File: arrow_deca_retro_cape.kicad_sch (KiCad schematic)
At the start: 48 parts, among them J1 ZXSP_ED2X28_SPE_SOL_EDGE, J10 Conn_02x05_Odd_Even, J11 Conn_01x04, J12 Conn_01x03, J13 Conn_01x01, J14 Conn_01x02, J15 Conn_01x03, J16 Conn_01x06, J2 Conn_01x03, J3 Conn_01x03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

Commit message: added Deto pmod
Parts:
- J16: footprint (none) -> Connector_PinHeader_2.54mm:PinHeader_1x06_P2.54mm_Vertical
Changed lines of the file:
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@@
   (symbol (lib_id "power:+3V3") (at 111.76 139.7 0) (unit 1)
     (in_bom yes) (on_board yes)
-    (property "Reference" "#PWR?" (id 0) (at 111.76 143.51 0)
+    (property "Reference" "#PWR031" (id 0) (at 111.76 143.51 0)
       (effects (font (size 1.27 1.27)) hide)
     )
@@
       (effects (font (size 1.27 1.27)) (justify left))
     )
-    (property "Footprint" "" (id 2) (at 118.745 147.32 0)
+    (property "Footprint" "Connector_PinHeader_2.54mm:PinHeader_1x06_P2.54mm_Vertical" (id 2) (at 118.745 147.32 0)
       (effects (font (size 1.27 1.27)) hide)
     )
@@
       (reference "#PWR030") (unit 1) (value "+2V5") (footprint "")
     )
+    (path "/2c197801-fcda-427b-8b74-c13df53c8843"
+      (reference "#PWR031") (unit 1) (value "+3V3") (footprint "")
+    )
     (path "/a40aa6c1-da40-4892-8d84-7e2be4c1f25d"
       (reference "#PWR0101") (unit 1) (value "GND") (footprint "")
@@
       (reference "#PWR0122") (unit 1) (value "GNDA") (footprint "")
     )
-    (path "/2c197801-fcda-427b-8b74-c13df53c8843"
-      (reference "#PWR?") (unit 1) (value "+3V3") (footprint "")
-    )
     (path "/00000000-0000-0000-0000-000061566687"
       (reference "C1") (unit 1) (value "1uF") (footprint "Capacitor_SMD:C_0603_1608Metric_Pad1.05x0.95mm_HandSolder")
@@
     )
     (path "/7d86abca-ab79-4536-9060-e252a4e431a0"
-      (reference "J16") (unit 1) (value "Conn_01x06") (footprint "")
+      (reference "J16") (unit 1) (value "Conn_01x06") (footprint "Connector_PinHeader_2.54mm:PinHeader_1x06_P2.54mm_Vertical")
     )
     (path "/439aafdc-2c0e-44db-ab96-7212e6daa700"

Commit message: v0.5 routing finalized
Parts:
- removed J11: Conn_01x04, Connector_PinSocket_2.54mm:PinSocket_1x04_P2.54mm_Vertical, symbol Connector_Generic:Conn_01x04
- added C21: 100uF, Capacitor_SMD:C_0805_2012Metric_Pad1.18x1.45mm_HandSolder, symbol Device:C
- added J11: USB_A, Connector_USB:USB_A_Molex_67643_Horizontal, symbol Connector:USB_A
- C20: value 0.1uF -> 10uF
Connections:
- net +2V5: now also C21.1
- net +5V: now also J11.1 (VBUS)
- net GND: now also C21.2, J11.4 (GND), J11.5 (Shield)
- net PS2_KEYB_CLK: now also R1.1; no longer R2.1
- net PS2_KEYB_DAT: now also R2.1; no longer R1.1
- net USB_D-_DM: now reaches D1.3, R2.2, R3.1
- net USB_D-_DM: now also J11.2 (D-)
- net USB_D+_DP: now reaches D2.3, R1.2, R4.1
- net USB_D+_DP: now also J11.3 (D+)
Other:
- note added: "- LOGOS I SILKSCREEN FRONT/BACK - USB3 SERIAL - REVISAR PINOUT I2S"
- note added: "USB"
- note removed: "ALTERNATIVA AMS1117-3V3 1A"
- note removed: "D+ / DP"
- note removed: "D- / DM"
- note removed: "UNIFICAR CONDENSADORS 0805 A 0603"
- note removed: "USB Header"
- company: (none) -> Hard Team Deca
- title: (none) -> DECA RETRO CAPE 1
- moved on the sheet: J10, J13, J14, J15

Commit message: update before split
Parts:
- removed J11: USB_A, Connector_USB:USB_A_Molex_67643_Horizontal, symbol Connector:USB_A
- R1, R2: value 510 -> 120; Field4 (none) -> Antonio entre 120 i 180 Ohm (47 també)
- R3, R4: value 4k7 -> NC
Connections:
- net +3V3: no longer J5.4
- net +5V: now also J5.4
- net PS2_KEYB_CLK: no longer J5.5
- net PS2_KEYB_DAT: no longer J5.1
- net USB_D+_DP: no longer names the net of D2.3, R1.2, R4.1
- net USB_D+_DP: now also J5.5
- net USB_D-_DM: no longer names the net of D1.3, R2.2, R3.1
- net USB_D-_DM: now also J5.1
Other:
- note added: "- REVISAR PINOUT, i2s retorn deca a DAC DETO 2, 3, 4 - USB3 SERIAL - I2S header al DETO PMOD - PS2 MOUSE connector - PULL DOWN PS2 GND POSAR A SORTIDES FPGA - REVISAR PULL DOWN CKE"
- note added: "BCLK"
- note added: "D+_DP"
- note added: "D-_DM"
- note added: "DIN"
- note added: "LRCLK"
- note removed: "- LOGOS I SILKSCREEN FRONT/BACK - USB3 SERIAL - REVISAR PINOUT I2S"
- note removed: "USB"
- moved on the sheet: D1, D2, J5, R1, R2, R3, R4

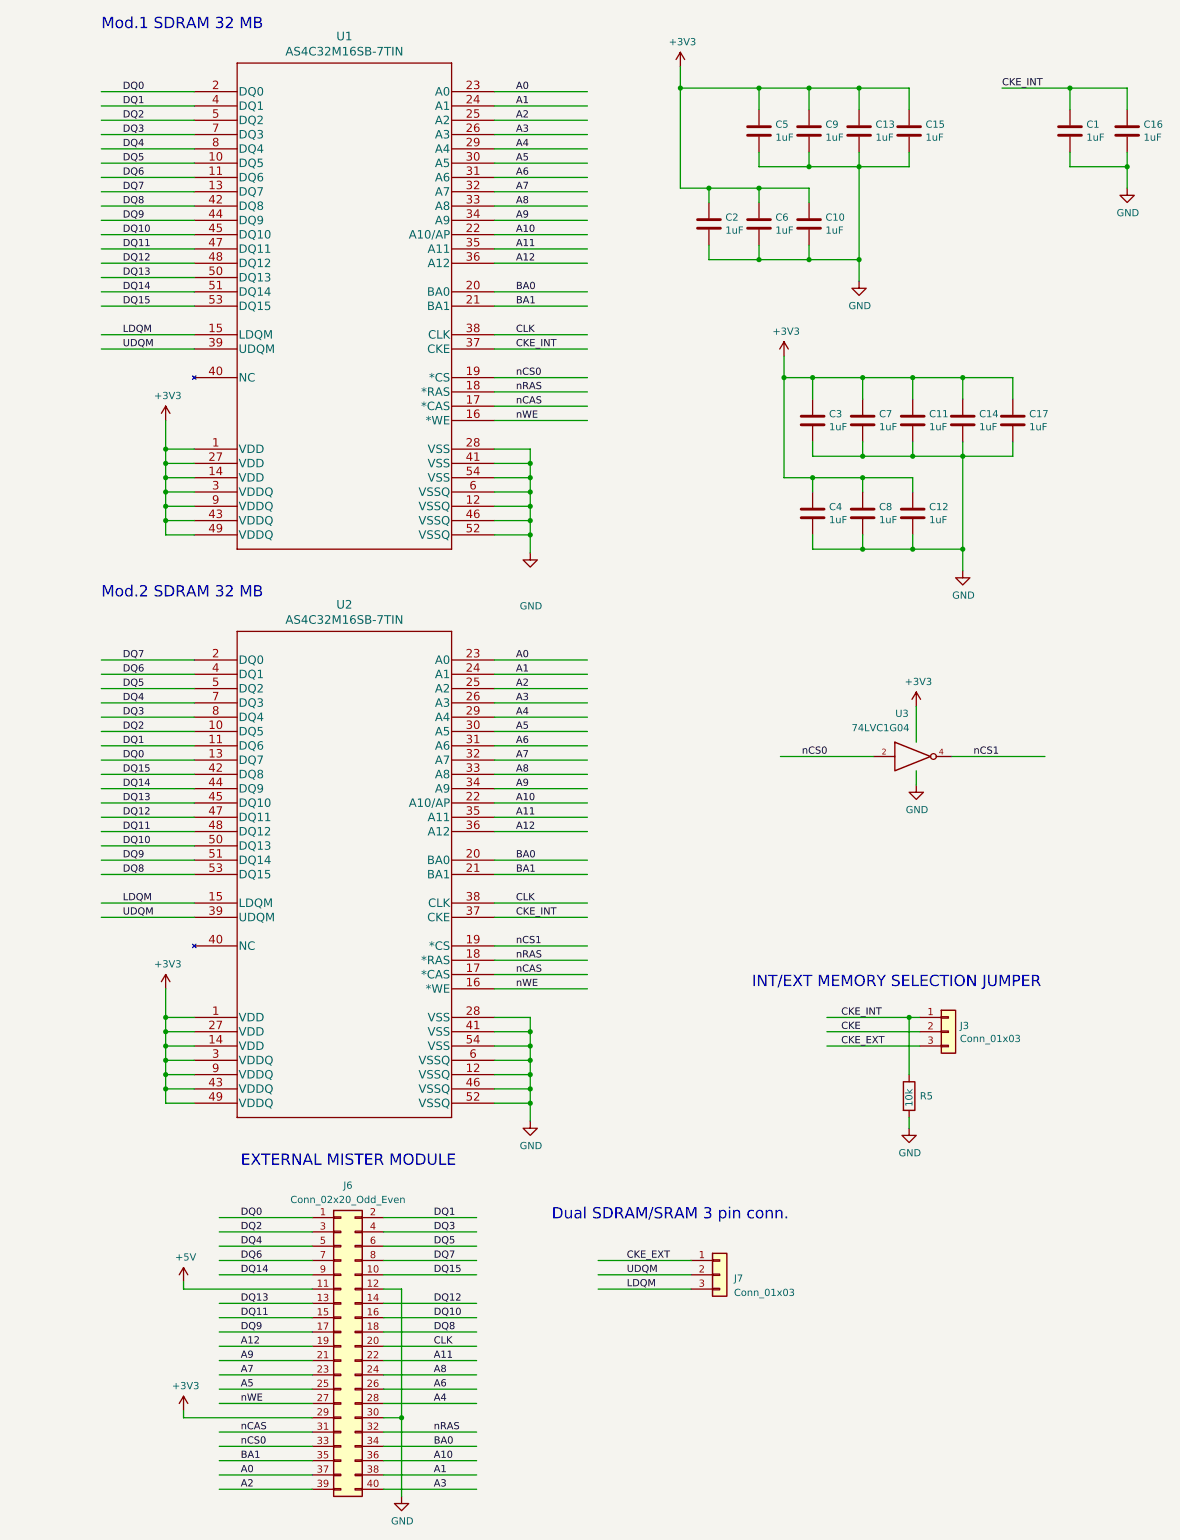
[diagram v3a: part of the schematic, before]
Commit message: v0.6 embedded SDRAM only version
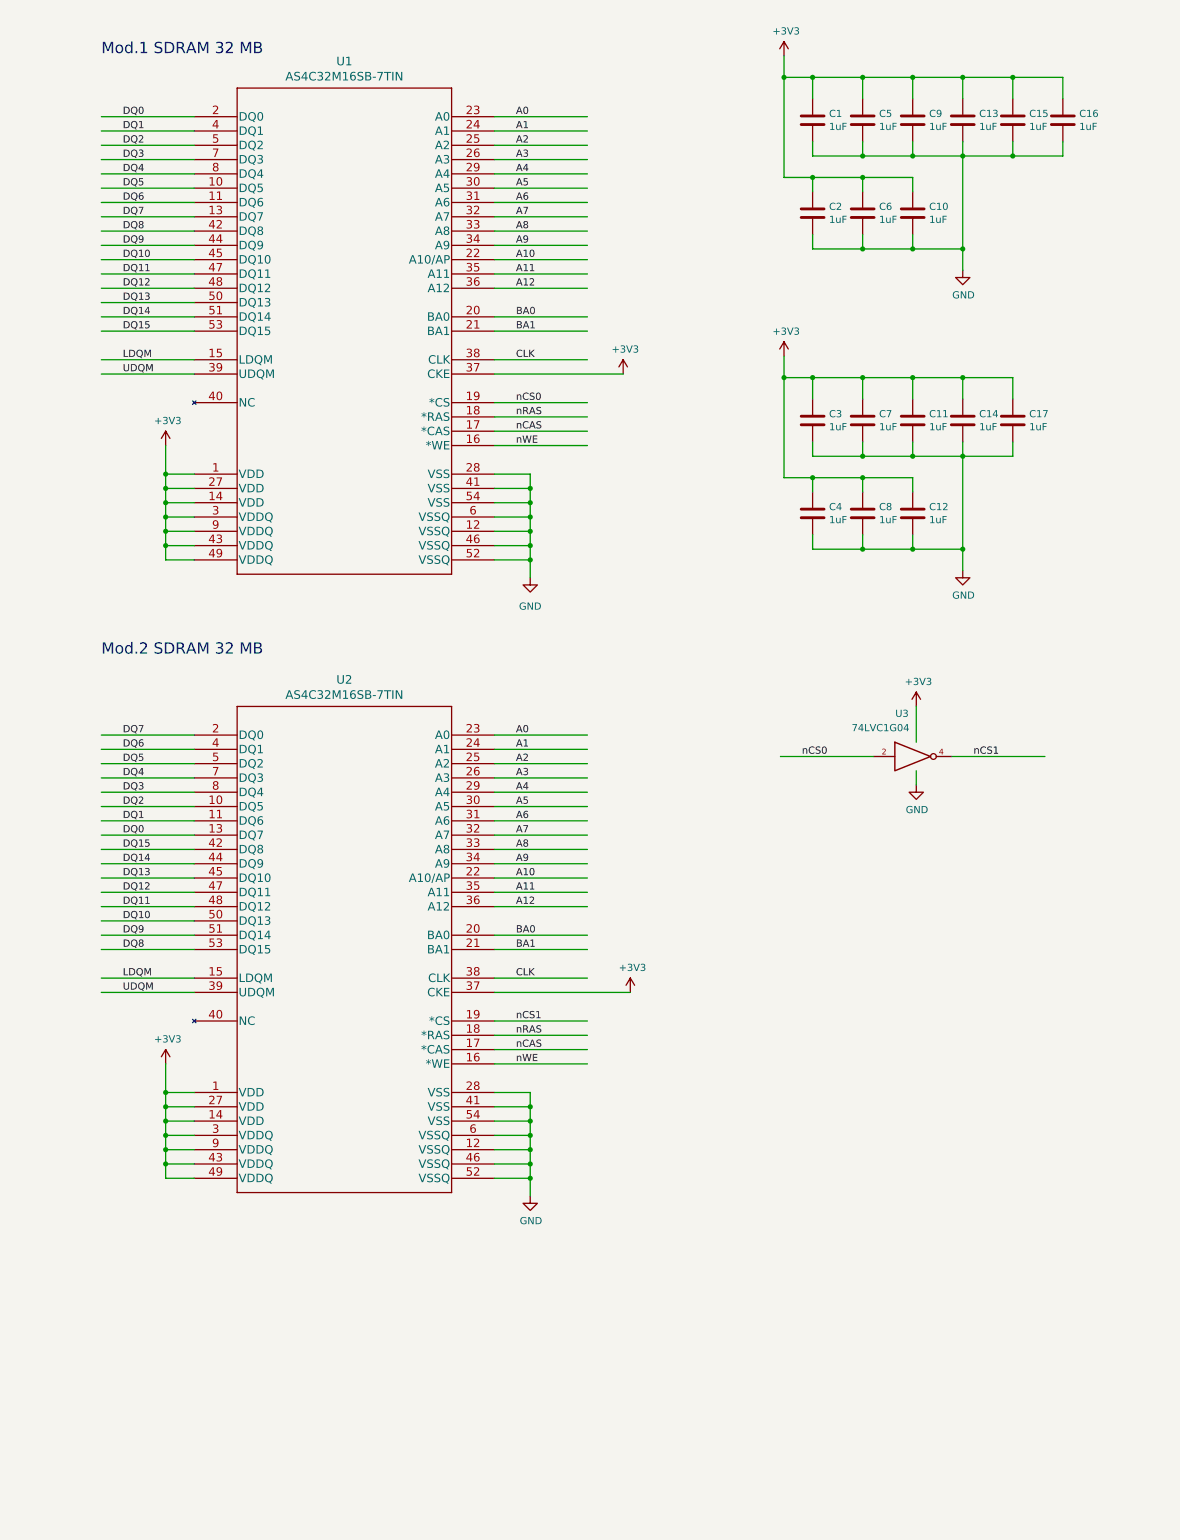
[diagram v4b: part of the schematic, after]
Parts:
- removed J3: Conn_01x03, Connector_PinHeader_2.54mm:PinHeader_1x03_P2.54mm_Vertical, symbol Connector_Generic:Conn_01x03
- removed J6: Conn_02x20_Odd_Even, Connector_PinHeader_2.54mm:PinHeader_2x20_P2.54mm_Vertical, symbol Connector_Generic:Conn_02x20_Odd_Even
- removed J7: Conn_01x03, Connector_PinSocket_2.54mm:PinSocket_1x03_P2.54mm_Vertical, symbol Connector_Generic:Conn_01x03
- removed R5: 10k, Resistor_SMD:R_0805_2012Metric_Pad1.20x1.40mm_HandSolder, symbol Device:R
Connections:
- net CKE_INT is gone; now on net +3V3: C1.1, C16.1, U1.37 (CKE), U2.37 (CKE)
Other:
- note removed: "Dual SDRAM/SRAM 3 pin conn."
- note removed: "EXTERNAL MISTER MODULE"
- note removed: "INT/EXT MEMORY SELECTION JUMPER"
- moved on the sheet: C1, C10, C13, C15, C16, C2, C5, C6, C9, U1, U2
